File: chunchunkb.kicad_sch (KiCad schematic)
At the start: 124 parts, among them J1 BATT, J2 OLED, SW1 SW_Push, SW10 SW_Push, SW11 SW_Push, SW12 SW_Push, SW13 SW_Push, SW14 SW_Push, SW15 SW_Push, SW16 SW_Push, SW17 SW_Push, SW18 SW_Push, SW19 SW_Push, SW2 SW_Push, SW20 SW_Push, SW21 SW_Push, SW22 SW_Push, SW23 SW_Push, SW24 SW_Push, SW25 SW_Push, SW26 SW_Push, SW27 SW_Push, SW28 SW_Push, SW29 SW_Push, SW3 SW_Push, SW30 SW_Push, SW31 EC11, SW32 SW_Push, SW33 SW_Push, SW34 SW_Push, SW35 SW_Push, SW36 SW_Push, SW4 SW_Push, SW5 SW_Push, SW6 SW_Push, SW7 SW_Push, SW8 SW_Push, SW9 SW_Push

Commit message: Merge pull request #2 from qwerty22121998/feat/rev2
feat: rev 2 board
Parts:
- added LED36: YS-SK6812MINI-E, chunchunkb:YS-SK6812MINI-E, symbol kbd:YS-SK6812MINI-E
- SW31: footprint chunchunkb:EC11_Switch -> chunchunkb:EC11_MX_Hybrid
- U1: footprint chunchunkb:ProMicro DUAL -> chunchunkb:ProMicro_DUAL
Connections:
- net GND: now also LED36.3 (GND)
- net VCC: now also LED36.1 (VDD)
- net at LED35.2 (DOUT): now also LED36.4 (DIN)
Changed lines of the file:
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@@
 	)
 	(no_connect
-		(at 281.94 118.11)
+		(at 269.24 118.11)
 	)
 	(no_connect
@@
 	)
 	(symbol
+		(lib_name "YS-SK6812MINI-E_35")
+		(lib_id "kbd:YS-SK6812MINI-E")
+		(at 275.59 118.11 0)
+		(mirror y)
+		(unit 1)
+		(body_style 1)
+		(exclude_from_sim no)
+		(in_bom yes)
+		(on_board yes)
+		(in_pos_files yes)
+		(dnp no)
+		(fields_autoplaced yes)
+		(property "Reference" "LED36"
+			(at 275.59 107.95 0)
+			(show_name no)
+			(do_not_autoplace no)
+			(effects
+				(font
+					(size 0.7366 0.7366)
+				)
+			)
+		)
+		(property "Value" "YS-SK6812MINI-E"
+			(at 275.59 110.49 0)
+			(show_name no)
+			(do_not_autoplace no)
+			(effects
+				(font
+					(size 0.7366 0.7366)
+				)
+			)
+		)
+		(property "Footprint" "chunchunkb:YS-SK6812MINI-E"
+			(at 273.05 124.46 0)
+			(hide yes)
+			(show_name no)
+			(do_not_autoplace no)
+			(effects
+				(font
+					(size 1.27 1.27)
+				)
+			)
+		)
+		(property "Datasheet" ""
+			(at 273.05 124.46 0)
+			(hide yes)
+			(show_name no)
+			(do_not_autoplace no)
+			(effects
+				(font
+					(size 1.27 1.27)
+				)
+			)
+		)
+		(property "Description" ""
+			(at 275.59 118.11 0)
+			(hide yes)
+			(show_name no)
+			(do_not_autoplace no)
+			(effects
+				(font
+					(size 1.27 1.27)
+				)
+			)
+		)
+		(pin "1"
+		)
+		(pin "4"
+		)
+		(pin "3"
+		)
+		(pin "2"
+		)
+		(instances
+			(project "chunchunkb"
+				(path "/c64465b6-eb49-4a63-b501-311556755a54"
+					(reference "LED36")
+					(unit 1)
+				)
+			)
+		)
+	)
+	(symbol
 		(lib_id "Diode:1N4148W")
 		(at 208.28 83.82 270)
@@
 			)
 		)
-		(property "Footprint" "chunchunkb:ProMicro DUAL"
+		(property "Footprint" "chunchunkb:ProMicro_DUAL"
 			(at 102.87 115.57 90)
 			(hide yes)
@@
 			)
 		)
-		(property "Footprint" "chunchunkb:EC11_Switch"
+		(property "Footprint" "chunchunkb:EC11_MX_Hybrid"
 			(at 77.47 131.826 0)
 			(hide yes)
@@
 	(symbol
 		(lib_id "power:GND")
-		(at 292.1 124.46 0)
+		(at 275.59 124.46 0)
 		(mirror y)
 		(unit 1)
@@
 		(fields_autoplaced yes)
 		(property "Reference" "#PWR012"
-			(at 292.1 130.81 0)
+			(at 275.59 130.81 0)
 			(hide yes)
 			(show_name no)
@@
 		)
 		(property "Value" "GND"
-			(at 294.64 125.73 0)
+			(at 278.13 125.73 0)
 			(show_name no)
 			(do_not_autoplace no)
@@
 		)
 		(property "Footprint" ""
-			(at 292.1 124.46 0)
+			(at 275.59 124.46 0)
 			(hide yes)
 			(show_name no)
@@
 		)
 		(property "Datasheet" ""
-			(at 292.1 124.46 0)
+			(at 275.59 124.46 0)
 			(hide yes)
 			(show_name no)
@@
 		)
 		(property "Description" "Power symbol creates a global label with name \"GND\" , ground"
-			(at 292.1 124.46 0)
+			(at 275.59 124.46 0)
 			(hide yes)
 			(show_name no)
@@
 		(fields_autoplaced yes)
 		(property "Reference" "LED35"
-			(at 292.1 107.95 0)
+			(at 292.1 125.73 0)
 			(show_name no)
 			(do_not_autoplace no)
@@
 		)
 		(property "Value" "YS-SK6812MINI-E"
-			(at 292.1 110.49 0)
+			(at 292.1 128.27 0)
 			(show_name no)
 			(do_not_autoplace no)
@@
 		(fields_autoplaced yes)
 		(property "Reference" "LED25"
-			(at 275.59 110.49 0)
+			(at 275.59 92.71 0)
 			(show_name no)
 			(do_not_autoplace no)
@@
 		)
 		(property "Value" "YS-SK6812MINI-E"
-			(at 275.59 113.03 0)
+			(at 275.59 95.25 0)
 			(show_name no)
 			(do_not_autoplace no)

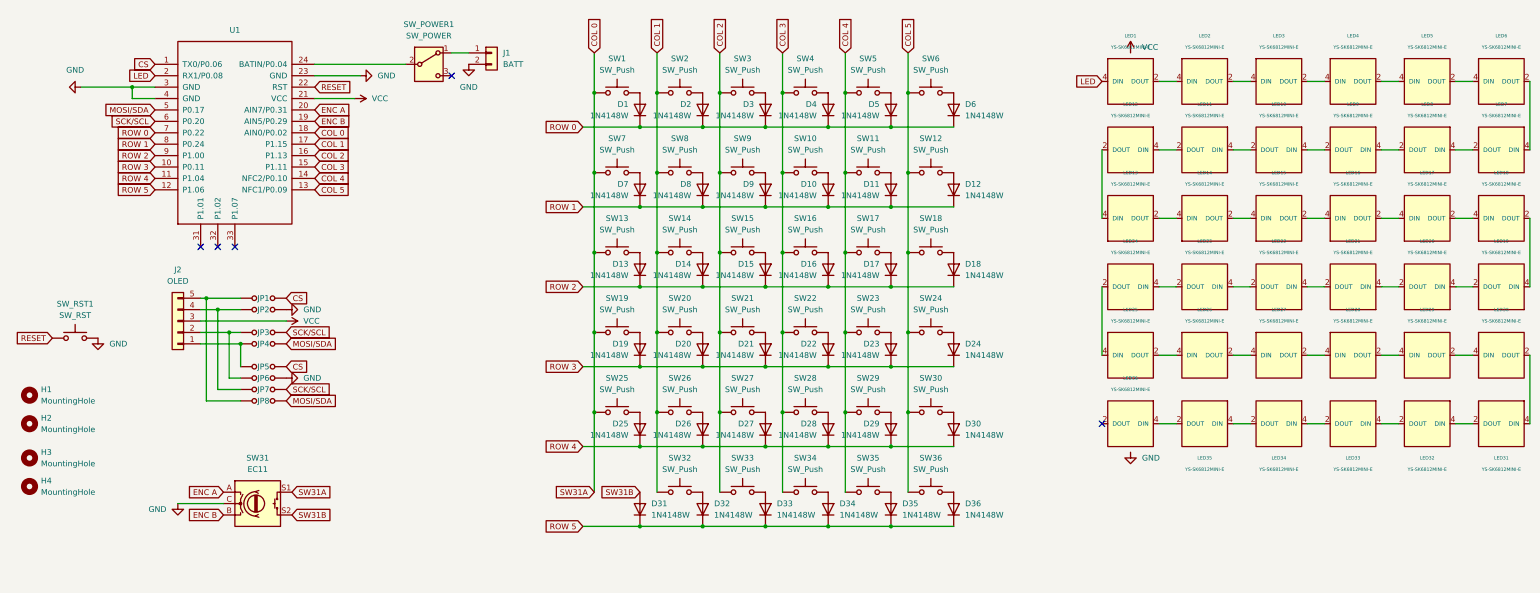
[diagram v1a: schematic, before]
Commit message: feat: rev 2 reversible PCB with full routing
- Replace the old symbol libs with chunchun_rev symbols and generated
  CC_* reversible footprints (tools/gen_footprints.py), using a jumper
  scheme and a right-half pin remap so one PCB serves both halves.
- Route the whole board: COL/ROW lanes by the nice!nano, VCC buses,
  GND fill with solid SMD connections and stitching vias.
- Add chunchunkb.kicad_dru (45-degree bends, no same-layer T-junctions)
  and tools/check_via_bends.py for the through-via bend rule KiCad's DRC
  cannot check.
- Diodes now put their cathodes on the ROW nets (col2row matrix).
- Add the plate STEP export for the case.
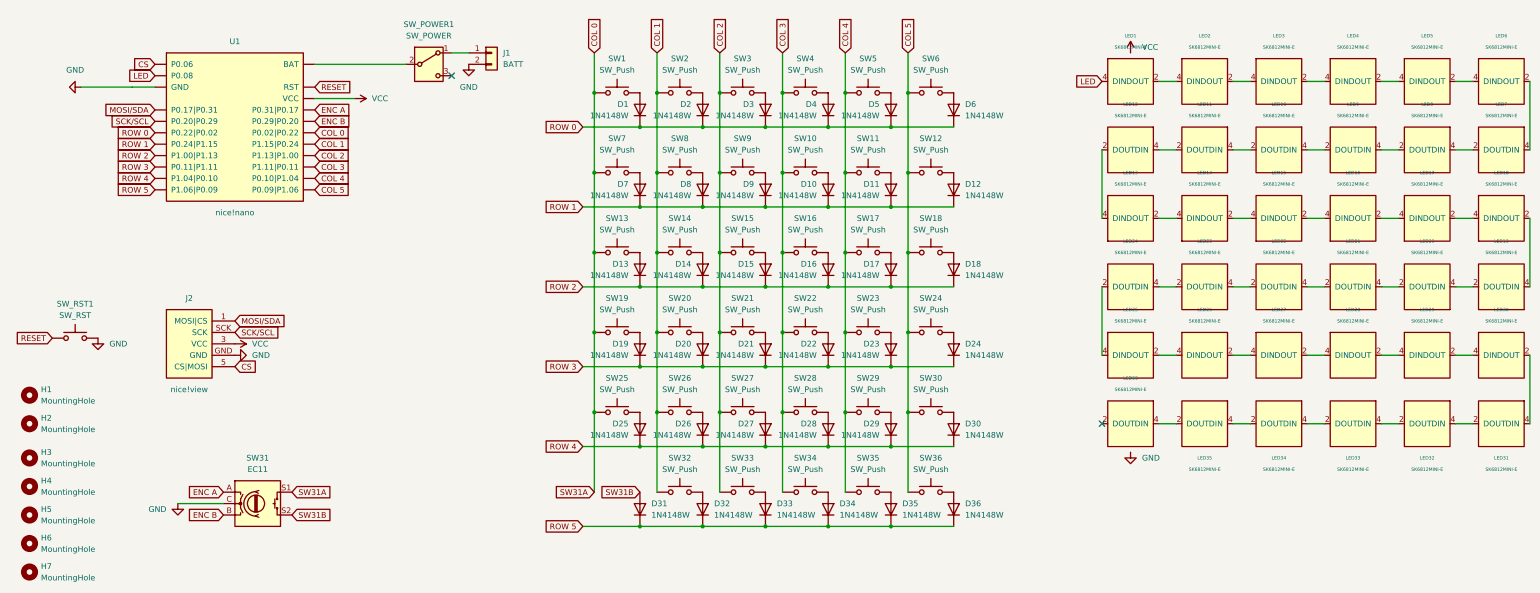
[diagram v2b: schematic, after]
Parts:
- removed JP1, JP2, JP3, JP4, JP5, JP6, JP7, JP8: jumper, chunchunkb:Jumper, symbol chunchunkb:jumper
- added H5, H6, H7: MountingHole, chunchun_rev:CC_Hole_4.1mm, symbol Mechanical:MountingHole
- D1, D10, D11, D12, D13, D14, D15, D16, D17, D18, D19, D2, D20, D21, D22, D23, D24, D25, D26, D27, D28, D29, D3, D30, D31, D32, D33, D34, D35, D36, D4, D5, D6, D7, D8, D9: footprint chunchunkb:crkbd-diode -> chunchun_rev:CC_D_SOD-123
- H1, H2, H3, H4: footprint chunchunkb:HOLE_M2_TH -> chunchun_rev:CC_Hole_4.1mm
- J1: footprint chunchunkb:MX1.25mm -> chunchun_rev:CC_Battery_MX1.25
- J2: value OLED -> nice!view; footprint chunchunkb:nice_view -> chunchun_rev:CC_Display_5pin; symbol Connector_Generic:Conn_01x05 -> chunchun_rev:CC_Display_5pin
- LED1, LED10, LED11, LED12, LED13, LED14, LED15, LED16, LED17, LED18, LED19, LED2, LED20, LED21, LED22, LED23, LED24, LED25, LED26, LED27, LED28, LED29, LED3, LED30, LED31, LED32, LED33, LED34, LED35, LED36, LED4, LED5, LED6, LED7, LED8, LED9: value YS-SK6812MINI-E -> SK6812MINI-E; footprint chunchunkb:YS-SK6812MINI-E -> chunchun_rev:CC_SK6812MINI-E; symbol kbd:YS-SK6812MINI-E -> chunchun_rev:CC_SK6812MINI-E
- SW1, SW10, SW11, SW12, SW13, SW14, SW15, SW16, SW17, SW18, SW19, SW2, SW20, SW21, SW22, SW23, SW24, SW25, SW26, SW27, SW28, SW29, SW3, SW30, SW32, SW33, SW34, SW35, SW36, SW4, SW5, SW6, SW7, SW8, SW9: footprint chunchunkb:MX-1U-Hotswap -> chunchun_rev:CC_MX_Hotswap_1u
- SW31: footprint chunchunkb:EC11_MX_Hybrid -> chunchun_rev:CC_EC11_MX_1u
- SW_POWER1: footprint chunchunkb:SW_SPDT_PCM12 -> chunchun_rev:CC_SW_Power_PCM12
- SW_RST1: footprint chunchunkb:SW_PUSH_1P1T_6x3.5mm_H4.3_APEM_MJTP1243 -> chunchun_rev:CC_SW_Reset
- U1: value (none) -> nice!nano; footprint chunchunkb:ProMicro_DUAL -> chunchun_rev:CC_nice_nano; symbol chunchunkb:nice_nano -> chunchun_rev:CC_nice_nano
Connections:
- net CS: now also J2.5 (CS|MOSI), U1.P0.06; no longer U1.1 (TX0/P0.06)
- net GND: now also J2.GND, U1.GND; no longer U1.23 (GND), U1.3 (GND), U1.4 (GND)
- net LED: now also U1.P0.08; no longer U1.2 (RX1/P0.08)
- net MOSI/SDA: now also J2.1 (MOSI|CS)
- net RESET: now also U1.RST; no longer U1.22 (RST)
- net SCK/SCL: now also J2.SCK
- net VCC: now also U1.VCC; no longer U1.21 (VCC)
- net at SW_POWER1.2 (B): now also U1.BAT; no longer U1.24 (BATIN/P0.04)
- no-connect marks 5 -> 2
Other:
- moved on the sheet: J2
